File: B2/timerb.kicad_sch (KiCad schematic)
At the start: 13 parts, among them U302 74HC04, U304 74HC32, U306 74HC08, U310 74HC00, U311 74HCT74, U312 74HC74, U313 74HC377, U314 74HC377, U315 74HC27, U316 74HC74, U317 74HC74, U318 74HC74, U319 74HC153

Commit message: Almost 0.1.1
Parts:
- renumbered U304 to U208, U317 to U209, U302 to U210, U315 to U211, U319 to U212, U316 to U213, U312 to U216, U318 to U217, U311 to U221, U314 to U224, U313 to U225, U310 to U226, U306 to U229
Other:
- title: 74HCT6526 Board 1 -> 74HCT6526 Board 2
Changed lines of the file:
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@@
   (paper "A4")
   (title_block
-    (title "74HCT6526 Board 1")
-    (date "2022-03-20")
-    (rev "0.0")
+    (title "74HCT6526 Board 2")
+    (date "2022-08-17")
+    (rev "0.1")
     (company "Daniel Molina")
     (comment 1 "https://github.com/dmolinagarcia/74HCT6526")
@@
   (symbol (lib_id "74xx:74HC74") (at 213.36 39.37 0) (unit 2)
     (in_bom yes) (on_board yes)
-    (property "Reference" "U318" (id 0) (at 211.455 39.37 0)
+    (property "Reference" "U217" (id 0) (at 211.455 39.37 0)
       (effects (font (size 1.27 1.27)) (justify left))
     )
@@
   (symbol (lib_id "74xx:74HC74") (at 59.69 29.21 0) (unit 2)
     (in_bom yes) (on_board yes)
-    (property "Reference" "U311" (id 0) (at 58.42 29.21 0)
+    (property "Reference" "U221" (id 0) (at 58.42 29.21 0)
       (effects (font (size 1.27 1.27)) (justify left))
     )
@@
   (symbol (lib_id "74xx:74HC00") (at 62.23 134.62 0) (unit 3)
     (in_bom yes) (on_board yes)
-    (property "Reference" "U310" (id 0) (at 62.23 134.62 0))
+    (property "Reference" "U226" (id 0) (at 62.23 134.62 0))
     (property "Value" "74HC00" (id 1) (at 62.23 129.6186 0))
     (property "Footprint" "Package_SO:SO-14_3.9x8.65mm_P1.27mm" (id 2) (at 62.23 134.62 0)
@@
   (symbol (lib_id "74xx:74LS27") (at 172.72 41.91 0) (unit 1)
     (in_bom yes) (on_board yes)
-    (property "Reference" "U315" (id 0) (at 172.72 41.91 0))
+    (property "Reference" "U211" (id 0) (at 172.72 41.91 0))
     (property "Value" "74HC27" (id 1) (at 172.72 36.9086 0))
     (property "Footprint" "Package_SO:SO-14_3.9x8.65mm_P1.27mm" (id 2) (at 172.72 41.91 0)
@@
   (symbol (lib_id "74xx:74HC74") (at 222.25 115.57 0) (unit 2)
     (in_bom yes) (on_board yes) (fields_autoplaced)
-    (property "Reference" "U317" (id 0) (at 224.2694 106.5235 0)
+    (property "Reference" "U209" (id 0) (at 224.2694 106.5235 0)
       (effects (font (size 1.27 1.27)) (justify left))
     )
@@
   (symbol (lib_id "74xx:74HC74") (at 80.01 29.21 0) (unit 1)
     (in_bom yes) (on_board yes)
-    (property "Reference" "U312" (id 0) (at 78.74 29.21 0)
+    (property "Reference" "U216" (id 0) (at 78.74 29.21 0)
       (effects (font (size 1.27 1.27)) (justify left))
     )
@@
   (symbol (lib_id "74xx:74LS32") (at 45.72 153.67 0) (unit 1)
     (in_bom yes) (on_board yes)
-    (property "Reference" "U304" (id 0) (at 45.72 153.67 0))
+    (property "Reference" "U208" (id 0) (at 45.72 153.67 0))
     (property "Value" "74HC32" (id 1) (at 45.72 148.6686 0))
     (property "Footprint" "Package_SO:SOIC-14_3.9x8.7mm_P1.27mm" (id 2) (at 45.72 153.67 0)
@@
   (symbol (lib_id "74xx:74LS153") (at 257.81 81.28 0) (unit 1)
     (in_bom yes) (on_board yes) (fields_autoplaced)
-    (property "Reference" "U319" (id 0) (at 259.8294 56.9935 0)
+    (property "Reference" "U212" (id 0) (at 259.8294 56.9935 0)
       (effects (font (size 1.27 1.27)) (justify left))
     )
@@
   (symbol (lib_id "74xx:74HC04") (at 167.64 69.85 0) (unit 6)
     (in_bom yes) (on_board yes)
-    (property "Reference" "U302" (id 0) (at 165.1 69.85 0)
+    (property "Reference" "U210" (id 0) (at 165.1 69.85 0)
       (effects (font (size 1.27 1.27)) (justify left))
     )
@@
   (symbol (lib_id "74xx:74HC00") (at 62.23 91.44 0) (unit 2)
     (in_bom yes) (on_board yes)
-    (property "Reference" "U310" (id 0) (at 62.23 91.44 0))
+    (property "Reference" "U226" (id 0) (at 62.23 91.44 0))
     (property "Value" "74HC00" (id 1) (at 62.23 86.4386 0))
     (property "Footprint" "Package_SO:SO-14_3.9x8.65mm_P1.27mm" (id 2) (at 62.23 91.44 0)
@@
   (symbol (lib_id "74xx:74HC74") (at 246.38 26.67 0) (unit 1)
     (in_bom yes) (on_board yes) (fields_autoplaced)
-    (property "Reference" "U318" (id 0) (at 248.3994 17.6235 0)
+    (property "Reference" "U217" (id 0) (at 248.3994 17.6235 0)
       (effects (font (size 1.27 1.27)) (justify left))
     )
@@
   (symbol (lib_id "Custom 74xx:74HC08") (at 234.95 44.45 0) (unit 2)
     (in_bom yes) (on_board yes)
-    (property "Reference" "U306" (id 0) (at 234.95 44.45 0))
+    (property "Reference" "U229" (id 0) (at 234.95 44.45 0))
     (property "Value" "74HC08" (id 1) (at 234.95 46.99 0))
     (property "Footprint" "Package_SO:SO-14_3.9x8.65mm_P1.27mm" (id 2) (at 234.95 44.45 0)
@@
   (symbol (lib_id "74xx:74HC74") (at 190.5 105.41 0) (unit 1)
     (in_bom yes) (on_board yes) (fields_autoplaced)
-    (property "Reference" "U317" (id 0) (at 192.5194 96.3635 0)
+    (property "Reference" "U209" (id 0) (at 192.5194 96.3635 0)
       (effects (font (size 1.27 1.27)) (justify left))
     )
@@
   (symbol (lib_id "74xx:74HC74") (at 190.5 81.28 0) (unit 1)
     (in_bom yes) (on_board yes)
-    (property "Reference" "U316" (id 0) (at 193.04 72.39 0)
+    (property "Reference" "U213" (id 0) (at 193.04 72.39 0)
       (effects (font (size 1.27 1.27)) (justify left))
     )
@@
   (symbol (lib_id "74xx:74LS27") (at 193.04 39.37 0) (unit 3)
     (in_bom yes) (on_board yes) (fields_autoplaced)
-    (property "Reference" "U315" (id 0) (at 193.04 31.5935 0))
+    (property "Reference" "U211" (id 0) (at 193.04 31.5935 0))
     (property "Value" "74HC27" (id 1) (at 193.04 34.3686 0))
     (property "Footprint" "Package_SO:SO-14_3.9x8.65mm_P1.27mm" (id 2) (at 193.04 39.37 0)
@@
   (symbol (lib_id "Custom 74xx:74HC08") (at 266.7 21.59 0) (unit 4)
     (in_bom yes) (on_board yes)
-    (property "Reference" "U306" (id 0) (at 266.065 20.955 0))
+    (property "Reference" "U229" (id 0) (at 266.065 20.955 0))
     (property "Value" "74HC08" (id 1) (at 266.7 16.5886 0))
     (property "Footprint" "Package_SO:SO-14_3.9x8.65mm_P1.27mm" (id 2) (at 266.7 21.59 0)
@@
   (symbol (lib_id "74xx:74LS377") (at 99.06 127 0) (unit 1)
     (in_bom yes) (on_board yes) (fields_autoplaced)
-    (property "Reference" "U314" (id 0) (at 101.0794 107.7935 0)
+    (property "Reference" "U224" (id 0) (at 101.0794 107.7935 0)
       (effects (font (size 1.27 1.27)) (justify left))
     )
@@
   (symbol (lib_id "74xx:74HC00") (at 46.99 88.9 0) (unit 1)
     (in_bom yes) (on_board yes)
-    (property "Reference" "U310" (id 0) (at 46.99 88.9 0))
+    (property "Reference" "U226" (id 0) (at 46.99 88.9 0))
     (property "Value" "74HC00" (id 1) (at 46.99 83.8986 0))
     (property "Footprint" "Package_SO:SO-14_3.9x8.65mm_P1.27mm" (id 2) (at 46.99 88.9 0)
@@
   (symbol (lib_id "74xx:74HC00") (at 46.99 137.16 0) (unit 4)
     (in_bom yes) (on_board yes)
-    (property "Reference" "U310" (id 0) (at 46.99 137.16 0))
+    (property "Reference" "U226" (id 0) (at 46.99 137.16 0))
     (property "Value" "74HC00" (id 1) (at 46.99 132.1586 0))
     (property "Footprint" "Package_SO:SO-14_3.9x8.65mm_P1.27mm" (id 2) (at 46.99 137.16 0)
@@
   (symbol (lib_id "74xx:74HC74") (at 36.83 29.21 0) (unit 1)
     (in_bom yes) (on_board yes)
-    (property "Reference" "U311" (id 0) (at 35.56 29.21 0)
+    (property "Reference" "U221" (id 0) (at 35.56 29.21 0)
       (effects (font (size 1.27 1.27)) (justify left))
     )
@@
   (symbol (lib_id "74xx:74HC74") (at 146.05 29.21 0) (unit 2)
     (in_bom yes) (on_board yes)
-    (property "Reference" "U312" (id 0) (at 144.78 29.21 0)
+    (property "Reference" "U216" (id 0) (at 144.78 29.21 0)
       (effects (font (size 1.27 1.27)) (justify left))
     )
@@
   (symbol (lib_id "74xx:74LS32") (at 45.72 168.91 0) (unit 2)
     (in_bom yes) (on_board yes)
-    (property "Reference" "U304" (id 0) (at 45.72 168.91 0))
+    (property "Reference" "U208" (id 0) (at 45.72 168.91 0))
     (property "Value" "74HC32" (id 1) (at 45.72 163.9086 0))
     (property "Footprint" "Package_SO:SOIC-14_3.9x8.7mm_P1.27mm" (id 2) (at 45.72 168.91 0)
@@
   (symbol (lib_id "74xx:74LS377") (at 99.06 78.74 0) (unit 1)
     (in_bom yes) (on_board yes) (fields_autoplaced)
-    (property "Reference" "U313" (id 0) (at 101.0794 59.5335 0)
+    (property "Reference" "U225" (id 0) (at 101.0794 59.5335 0)
       (effects (font (size 1.27 1.27)) (justify left))
     )
@@
   (symbol (lib_id "74xx:74LS27") (at 168.91 29.21 0) (unit 2)
     (in_bom yes) (on_board yes)
-    (property "Reference" "U315" (id 0) (at 168.91 29.21 0))
+    (property "Reference" "U211" (id 0) (at 168.91 29.21 0))
     (property "Value" "74HC27" (id 1) (at 168.402 34.798 0))
     (property "Footprint" "Package_SO:SO-14_3.9x8.65mm_P1.27mm" (id 2) (at 168.91 29.21 0)

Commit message: Added ICR. B2 fixes
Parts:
- U229: value 74HC08 -> 74HCT08
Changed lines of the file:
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@@
     (in_bom yes) (on_board yes)
     (property "Reference" "U229" (id 0) (at 234.95 44.45 0))
-    (property "Value" "74HC08" (id 1) (at 234.95 46.99 0))
+    (property "Value" "74HCT08" (id 1) (at 234.95 46.99 0))
     (property "Footprint" "Package_SO:SO-14_3.9x8.65mm_P1.27mm" (id 2) (at 234.95 44.45 0)
       (effects (font (size 1.27 1.27)) hide)
@@
     (in_bom yes) (on_board yes)
     (property "Reference" "U229" (id 0) (at 266.065 20.955 0))
-    (property "Value" "74HC08" (id 1) (at 266.7 16.5886 0))
+    (property "Value" "74HCT08" (id 1) (at 266.7 16.5886 0))
     (property "Footprint" "Package_SO:SO-14_3.9x8.65mm_P1.27mm" (id 2) (at 266.7 21.59 0)
       (effects (font (size 1.27 1.27)) hide)

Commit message: B0 ready for v0.2.0 release.
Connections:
- net at U221.10 (~{S}), U221.6 (~{Q}): no longer U221.1 (~{R})
- net at U221.8 (~{Q}): now also U221.1 (~{R})
- no-connect marks 8 -> 7
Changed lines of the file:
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@@
   (title_block
     (title "74HCT6526 Board 2")
-    (date "2022-10-08")
-    (rev "0.1.2")
+    (date "2023-01-22")
+    (rev "0.2.0")
     (company "Daniel Molina")
     (comment 1 "https://github.com/dmolinagarcia/74HCT6526")
@@
   (junction (at 30.48 86.36) (diameter 0) (color 0 0 0 0)
   )
-  (junction (at 46.99 31.75) (diameter 0) (color 0 0 0 0)
-  )
   (junction (at 135.89 53.34) (diameter 0) (color 0 0 0 0)
   )
@@
   )
   (no_connect (at 87.63 31.75))
-  (no_connect (at 67.31 31.75))
   (no_connect (at 44.45 26.67))
   (no_connect (at 270.51 81.28))
@@
     (stroke (width 0) (type default) (color 0 0 0 0))
   )
+  (wire (pts (xy 67.31 31.75) (xy 69.85 31.75))
+    (stroke (width 0) (type default) (color 0 0 0 0))
+  )
   (wire (pts (xy 46.99 31.75) (xy 46.99 20.32))
     (stroke (width 0) (type default) (color 0 0 0 0))
@@
     (stroke (width 0) (type default) (color 0 0 0 0))
   )
-  (wire (pts (xy 46.99 38.1) (xy 36.83 38.1))
+  (wire (pts (xy 36.83 38.1) (xy 69.85 38.1))
     (stroke (width 0) (type default) (color 0 0 0 0))
   )
@@
     (stroke (width 0) (type default) (color 0 0 0 0))
   )
-  (wire (pts (xy 46.99 31.75) (xy 46.99 38.1))
-    (stroke (width 0) (type default) (color 0 0 0 0))
-  )
   (wire (pts (xy 53.34 168.91) (xy 173.99 168.91))
     (stroke (width 0) (type default) (color 0 0 0 0))
@@
     (stroke (width 0) (type default) (color 0 0 0 0))
   )
+  (wire (pts (xy 69.85 31.75) (xy 69.85 38.1))
+    (stroke (width 0) (type default) (color 0 0 0 0))
+  )

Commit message: Ready for v0.2.1
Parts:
- removed unit 2 of U217
- added U230: 74HC74, Package_SO:SO-14_3.9x8.65mm_P1.27mm, symbol 74xx:74HC74
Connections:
- net TBLOAD: now also U211.9; no longer U211.10
- net TBPULSESET: now also U216.13 (~{R})
- net TBUNDERFLOW: now also U211.10; no longer U211.9
- net VCC: now also U230.10 (~{S}), U230.12 (D), U230.4 (~{S})
- net ~{PHI2}: now also U230.11 (C), U230.3 (C)
- net at U211.8: now also U230.1 (~{R}), U230.13 (~{R}); no longer U216.13 (~{R})
- net at U229.4: now also U230.5 (Q)
- new net: U230.2 (D), U230.9 (Q)
- no-connect marks 7 -> 8
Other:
- moved on the sheet: U229B

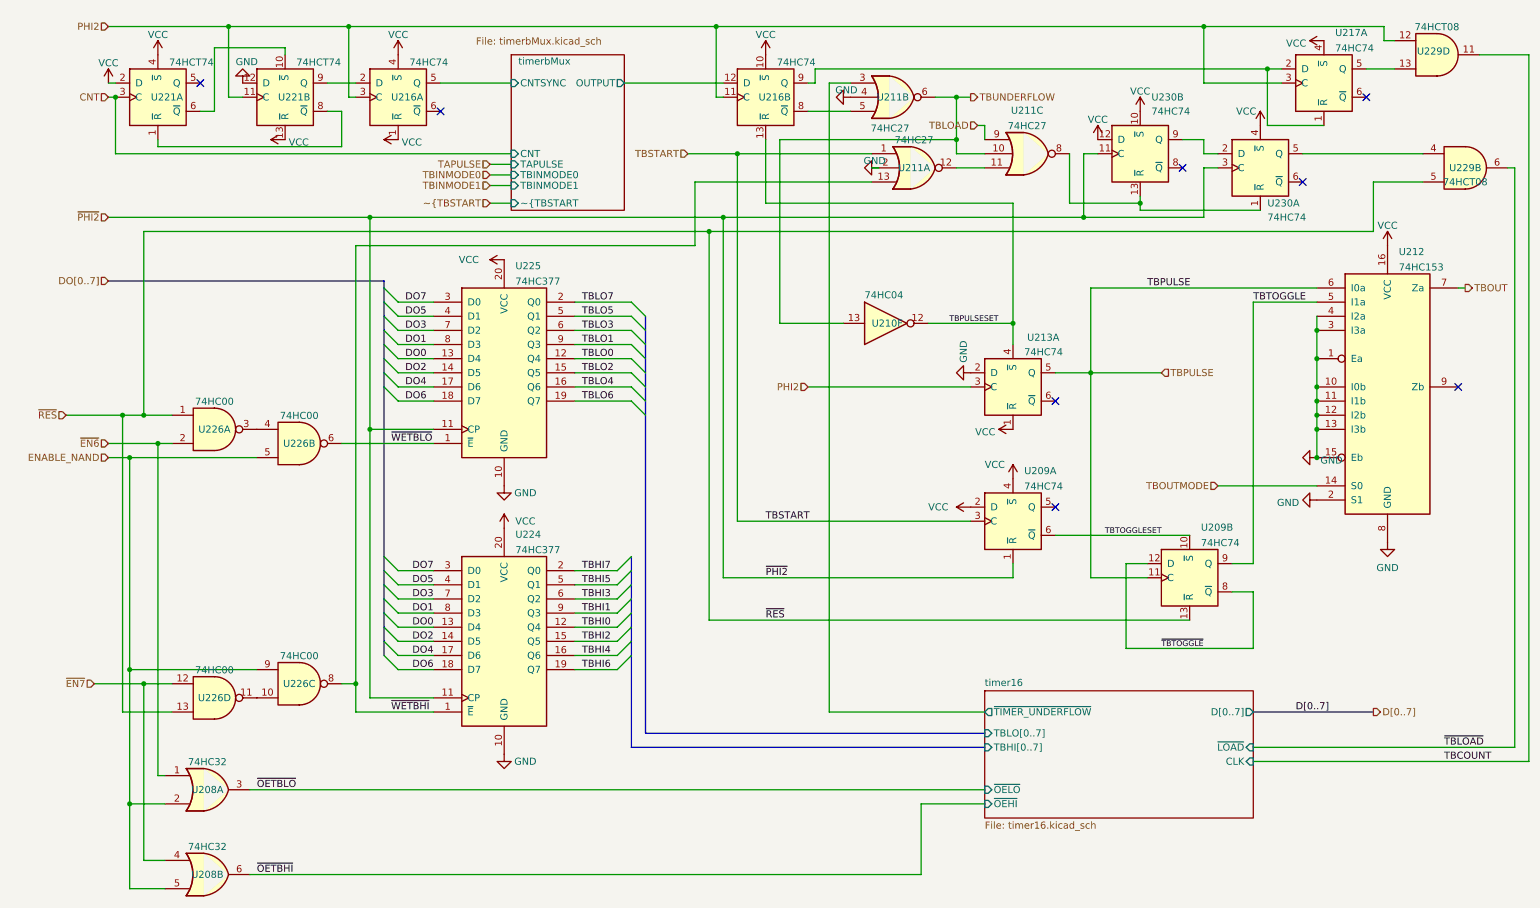
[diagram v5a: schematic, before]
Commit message: B2 refactored. B4 Added. TOD sch completed.
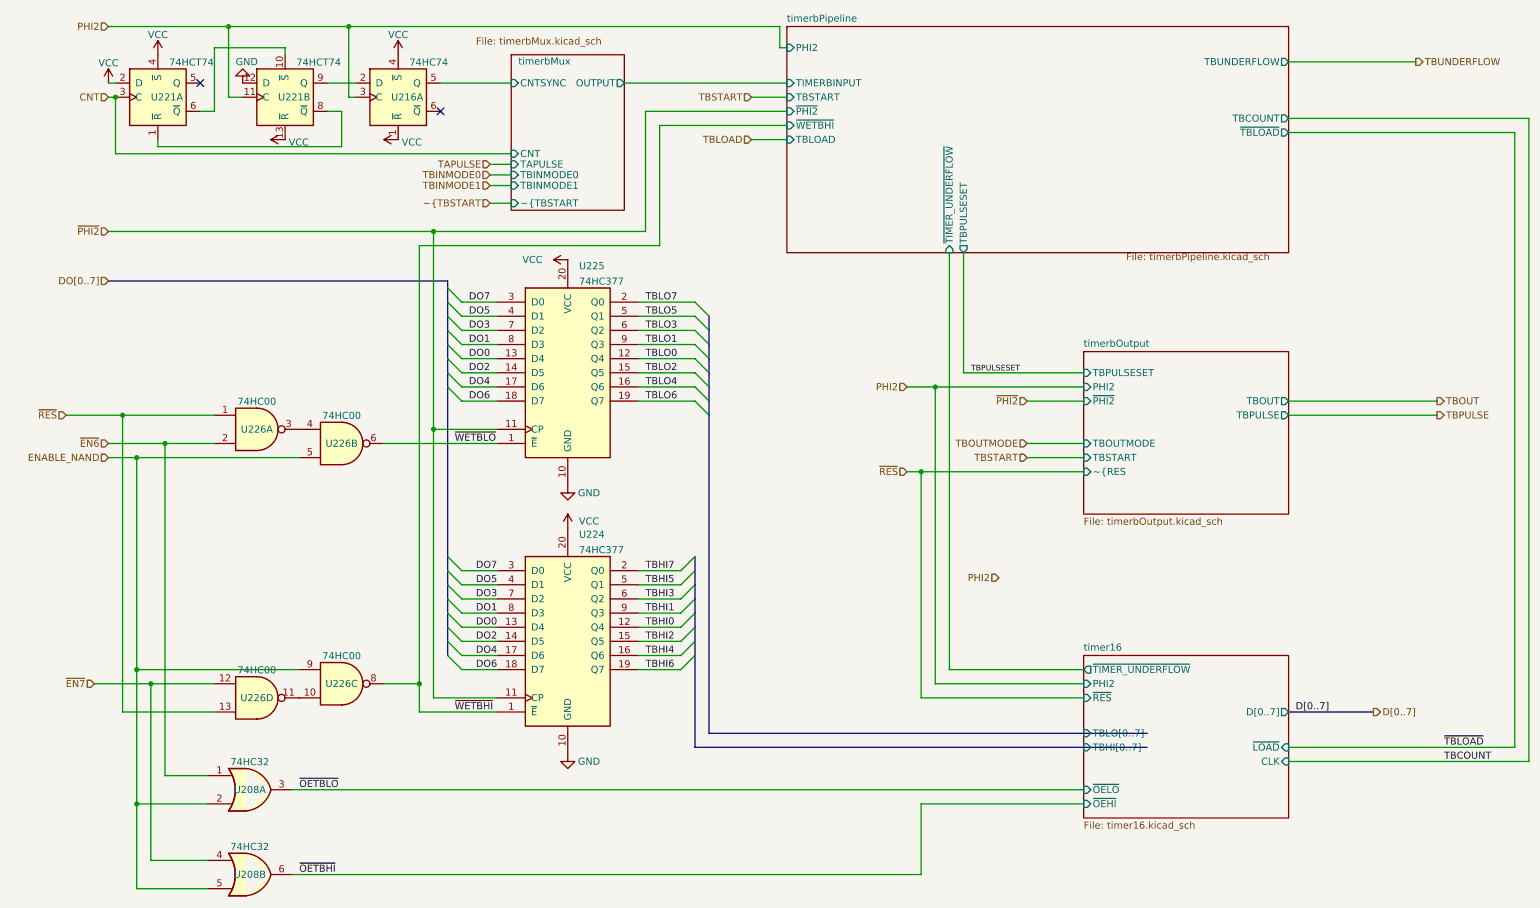
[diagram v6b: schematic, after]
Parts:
- removed U209, U213, U217, U230: 74HC74, Package_SO:SO-14_3.9x8.65mm_P1.27mm, symbol 74xx:74HC74
- removed U210: 74HC04, Package_SO:SOIC-14_3.9x8.7mm_P1.27mm, symbol 74xx:74HC04
- removed U211: 74HC27, Package_SO:SO-14_3.9x8.65mm_P1.27mm, symbol 74xx:74LS27
- removed U212: 74HC153, Package_SO:SOIC-16_3.9x9.9mm_P1.27mm, symbol 74xx:74LS153
- removed unit 2 of U216
- removed U229: 74HCT08, Package_SO:SO-14_3.9x8.65mm_P1.27mm, symbol Custom 74xx:74HC08
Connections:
- no-connect marks 8 -> 2
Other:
- added sheet timerbOutput (timerbOutput.kicad_sch)
- added sheet timerbPipeline (timerbPipeline.kicad_sch)
- sheet timer16 ports: added PHI2, ~{RES}; removed none
- moved on the sheet: U208A, U208B, U224, U225, U226A, U226B, U226C, U226D

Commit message: Ready for v0.2.2
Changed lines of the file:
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@@
   (title_block
     (title "74HCT6526 Board 2")
-    (date "2023-03-25")
-    (rev "0.2.1")
+    (date "2023-06-22")
+    (rev "0.2.2")
     (company "Daniel Molina")
     (comment 1 "https://github.com/dmolinagarcia/74HCT6526")
@@
     (stroke (width 0) (type default) (color 0 0 0 0))
   )
-  (bus (pts (xy 133.35 146.05) (xy 214.63 146.05))
-    (stroke (width 0) (type default) (color 0 0 0 0))
-  )
   (wire (pts (xy 83.82 134.62) (xy 83.82 139.7))
     (stroke (width 0) (type default) (color 0 0 0 0))
@@
     (stroke (width 0) (type default) (color 0 0 0 0))
   )
+  (bus (pts (xy 135.89 143.51) (xy 203.2 143.51))
+    (stroke (width 0) (type default) (color 0 0 0 0))
+  )
+  (bus (pts (xy 133.35 146.05) (xy 203.2 146.05))
+    (stroke (width 0) (type default) (color 0 0 0 0))
+  )
   (wire (pts (xy 83.82 55.88) (xy 83.82 134.62))
     (stroke (width 0) (type default) (color 0 0 0 0))
   )
   (wire (pts (xy 52.07 29.21) (xy 49.53 29.21))
-    (stroke (width 0) (type default) (color 0 0 0 0))
-  )
-  (bus (pts (xy 135.89 143.51) (xy 214.63 143.51))
     (stroke (width 0) (type default) (color 0 0 0 0))
   )
@@
     (effects (font (size 1.27 1.27)) (justify right))
   )
-  (hierarchical_label "PHI2" (shape input) (at 187.96 115.57 180)
-    (effects (font (size 1.27 1.27)) (justify right))
-  )
